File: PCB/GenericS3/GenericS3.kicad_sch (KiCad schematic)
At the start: 58 parts, among them J1 USB-C, J2 Shelly, P1 33, P10 42, P11 45, P12 46, P13 47, P14 48, P15 18, P16 19, P17 14, P18 15, P19 16, P2 34, P20 17, P21 6, P22 7, P23 8, P24 9, P25 20, P26 10, P27 11, P28 12, P29 13, P3 35, P30 1, P31 2, P32 3, P33 4, P34 5, P35 21, P36 43, P37 44, P38 0, P4 36, P5 37, P6 38, P7 39, P8 40, P9 41, U2 ESP32-S3-MINI-1, U5 MD8942

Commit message: Added GND pads
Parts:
- added P39, P40, P41, P42: ⏚, RevK:Square, symbol RevK:Square
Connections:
- net GND: now also P39.1 (P), P40.1 (P), P41.1 (P), P42.1 (P)
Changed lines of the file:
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@@
+    )
+  )
+  (symbol (lib_id "RevK:Square") (at 160.655 100.33 0) (unit 1)
+    (in_bom no) (on_board yes) (dnp no) (fields_autoplaced)
+    (property "Reference" "P42" (at 167.005 100.33 0)
+      (effects (font (size 1.27 1.27)) hide)
+    )
+    (property "Value" "⏚" (at 163.9062 100.33 0)
+      (effects (font (size 1.27 1.27)) (justify left))
+    )
+    (property "Footprint" "RevK:Square" (at 160.655 102.87 0)
+      (effects (font (size 1.27 1.27)) hide)
+    )
+    (property "Datasheet" "" (at 160.655 100.33 0)
+      (effects (font (size 1.27 1.27)) hide)
+    )
+    (pin "1")
+    (instances
+      (project "GenericS3"
+        (path "/2d210a96-f81f-42a9-8bf4-1b43c11086f3"
+          (reference "P42") (unit 1)
+        )
+      )
     )
   )
@@
         (path "/2d210a96-f81f-42a9-8bf4-1b43c11086f3"
           (reference "P11") (unit 1)
+        )
+      )
+    )
+  )
+  (symbol (lib_id "RevK:Square") (at 160.655 96.52 0) (unit 1)
+    (in_bom no) (on_board yes) (dnp no) (fields_autoplaced)
+    (property "Reference" "P41" (at 167.005 96.52 0)
+      (effects (font (size 1.27 1.27)) hide)
+    )
+    (property "Value" "⏚" (at 163.9062 96.52 0)
+      (effects (font (size 1.27 1.27)) (justify left))
+    )
+    (property "Footprint" "RevK:Square" (at 160.655 99.06 0)
+      (effects (font (size 1.27 1.27)) hide)
+    )
+    (property "Datasheet" "" (at 160.655 96.52 0)
+      (effects (font (size 1.27 1.27)) hide)
+    )
+    (pin "1")
+    (instances
+      (project "GenericS3"
+        (path "/2d210a96-f81f-42a9-8bf4-1b43c11086f3"
+          (reference "P41") (unit 1)
         )
       )
@@
     )
   )
+  (symbol (lib_id "power:GND") (at 160.655 88.9 270) (unit 1)
+    (in_bom yes) (on_board yes) (dnp no) (fields_autoplaced)
+    (property "Reference" "#PWR02" (at 154.305 88.9 0)
+      (effects (font (size 1.27 1.27)) hide)
+    )
+    (property "Value" "GND" (at 157.4801 88.9 90)
+      (effects (font (size 1.27 1.27)) (justify right))
+    )
+    (property "Footprint" "" (at 160.655 88.9 0)
+      (effects (font (size 1.27 1.27)) hide)
+    )
+    (property "Datasheet" "" (at 160.655 88.9 0)
+      (effects (font (size 1.27 1.27)) hide)
+    )
+    (pin "1")
+    (instances
+      (project "GenericS3"
+        (path "/2d210a96-f81f-42a9-8bf4-1b43c11086f3"
+          (reference "#PWR02") (unit 1)
+        )
+      )
+    )
+  )
   (symbol (lib_id "RevK:Round") (at 93.98 67.945 180) (unit 1)
     (in_bom no) (on_board yes) (dnp no)
@@
     )
   )
+  (symbol (lib_id "power:GND") (at 160.655 92.71 270) (unit 1)
+    (in_bom yes) (on_board yes) (dnp no) (fields_autoplaced)
+    (property "Reference" "#PWR05" (at 154.305 92.71 0)
+      (effects (font (size 1.27 1.27)) hide)
+    )
+    (property "Value" "GND" (at 157.4801 92.71 90)
+      (effects (font (size 1.27 1.27)) (justify right))
+    )
+    (property "Footprint" "" (at 160.655 92.71 0)
+      (effects (font (size 1.27 1.27)) hide)
+    )
+    (property "Datasheet" "" (at 160.655 92.71 0)
+      (effects (font (size 1.27 1.27)) hide)
+    )
+    (pin "1")
+    (instances
+      (project "GenericS3"
+        (path "/2d210a96-f81f-42a9-8bf4-1b43c11086f3"
+          (reference "#PWR05") (unit 1)
+        )
+      )
+    )
+  )
   (symbol (lib_id "RevK:VCUT") (at 250.19 169.545 0) (unit 1)
     (in_bom no) (on_board yes) (dnp no) (fields_autoplaced)
@@
     )
   )
+  (symbol (lib_id "power:GND") (at 160.655 96.52 270) (unit 1)
+    (in_bom yes) (on_board yes) (dnp no) (fields_autoplaced)
+    (property "Reference" "#PWR015" (at 154.305 96.52 0)
+      (effects (font (size 1.27 1.27)) hide)
+    )
+    (property "Value" "GND" (at 157.4801 96.52 90)
+      (effects (font (size 1.27 1.27)) (justify right))
+    )
+    (property "Footprint" "" (at 160.655 96.52 0)
+      (effects (font (size 1.27 1.27)) hide)
+    )
+    (property "Datasheet" "" (at 160.655 96.52 0)
+      (effects (font (size 1.27 1.27)) hide)
+    )
+    (pin "1")
+    (instances
+      (project "GenericS3"
+        (path "/2d210a96-f81f-42a9-8bf4-1b43c11086f3"
+          (reference "#PWR015") (unit 1)
+        )
+      )
+    )
+  )
   (symbol (lib_id "RevK:Round") (at 124.46 85.725 0) (unit 1)
     (in_bom no) (on_board yes) (dnp no) (fields_autoplaced)
@@
         (path "/2d210a96-f81f-42a9-8bf4-1b43c11086f3"
           (reference "P38") (unit 1)
+        )
+      )
+    )
+  )
+  (symbol (lib_id "RevK:Square") (at 160.655 92.71 0) (unit 1)
+    (in_bom no) (on_board yes) (dnp no) (fields_autoplaced)
+    (property "Reference" "P40" (at 167.005 92.71 0)
+      (effects (font (size 1.27 1.27)) hide)
+    )
+    (property "Value" "⏚" (at 163.9062 92.71 0)
+      (effects (font (size 1.27 1.27)) (justify left))
+    )
+    (property "Footprint" "RevK:Square" (at 160.655 95.25 0)
+      (effects (font (size 1.27 1.27)) hide)
+    )
+    (property "Datasheet" "" (at 160.655 92.71 0)
+      (effects (font (size 1.27 1.27)) hide)
+    )
+    (pin "1")
+    (instances
+      (project "GenericS3"
+        (path "/2d210a96-f81f-42a9-8bf4-1b43c11086f3"
+          (reference "P40") (unit 1)
         )
       )
@@
         (path "/825c70b0-4860-42b7-97dc-86bfa46e06fd"
           (reference "R7") (unit 1)
+        )
+      )
+    )
+  )
+  (symbol (lib_id "RevK:Square") (at 160.655 88.9 0) (unit 1)
+    (in_bom no) (on_board yes) (dnp no) (fields_autoplaced)
+    (property "Reference" "P39" (at 167.005 88.9 0)
+      (effects (font (size 1.27 1.27)) hide)
+    )
+    (property "Value" "⏚" (at 163.9062 88.9 0)
+      (effects (font (size 1.27 1.27)) (justify left))
+    )
+    (property "Footprint" "RevK:Square" (at 160.655 91.44 0)
+      (effects (font (size 1.27 1.27)) hide)
+    )
+    (property "Datasheet" "" (at 160.655 88.9 0)
+      (effects (font (size 1.27 1.27)) hide)
+    )
+    (pin "1")
+    (instances
+      (project "GenericS3"
+        (path "/2d210a96-f81f-42a9-8bf4-1b43c11086f3"
+          (reference "P39") (unit 1)
         )
       )
@@
         )
       )
+    )
+  )
+  (symbol (lib_id "power:GND") (at 160.655 100.33 270) (unit 1)
+    (in_bom yes) (on_board yes) (dnp no) (fields_autoplaced)
+    (property "Reference" "#PWR016" (at 154.305 100.33 0)
+      (effects (font (size 1.27 1.27)) hide)
+    )
+    (property "Value" "GND" (at 157.4801 100.33 90)
+      (effects (font (size 1.27 1.27)) (justify right))
+    )
+    (property "Footprint" "" (at 160.655 100.33 0)
+      (effects (font (size 1.27 1.27)) hide)
+    )
+    (property "Datasheet" "" (at 160.655 100.33 0)
+      (effects (font (size 1.27 1.27)) hide)
+    )
+    (pin "1")
+    (instances
+      (project "GenericS3"
+        (path "/2d210a96-f81f-42a9-8bf4-1b43c11086f3"
+          (reference "#PWR016") (unit 1)
+        )
+      )

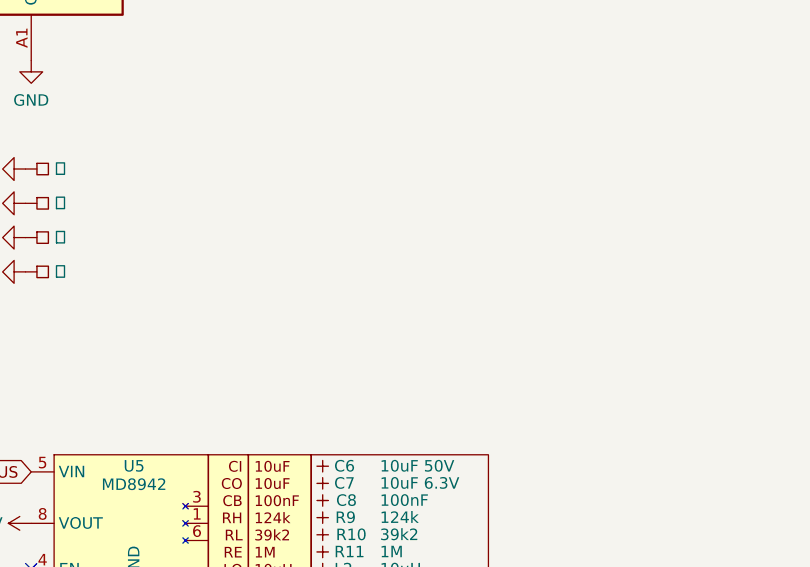
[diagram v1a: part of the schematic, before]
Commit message: Added connector
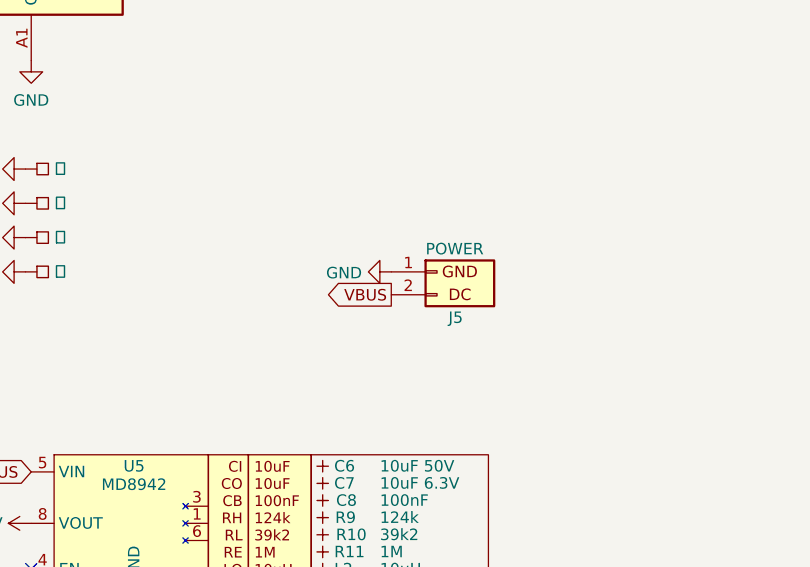
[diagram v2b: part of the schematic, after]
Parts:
- added J5: POWER, RevK:PTSM-HH1-2-RA, symbol RevK:PowerIn
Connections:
- net GND: now also J5.1 (GND)
- net VBUS: now also J5.2 (DC)
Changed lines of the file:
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@@
+    )
+  )
+  (global_label "VBUS" (shape output) (at 201.295 102.87 180) (fields_autoplaced)
+    (effects (font (size 1.27 1.27)) (justify right))
+    (property "Intersheetrefs" "${INTERSHEET_REFS}" (at 194.0654 102.87 0)
+      (effects (font (size 1.27 1.27)) (justify right) hide)
     )
   )
@@
     )
   )
+  (symbol (lib_id "RevK:PowerIn") (at 206.375 100.33 0) (unit 1)
+    (in_bom yes) (on_board yes) (dnp no)
+    (property "Reference" "J5" (at 207.645 105.41 0)
+      (effects (font (size 1.27 1.27)) (justify left))
+    )
+    (property "Value" "POWER" (at 205.105 97.79 0)
+      (effects (font (size 1.27 1.27)) (justify left))
+    )
+    (property "Footprint" "RevK:PTSM-HH1-2-RA" (at 206.375 100.33 0)
+      (effects (font (size 1.27 1.27)) hide)
+    )
+    (property "Datasheet" "~" (at 206.375 100.33 0)
+      (effects (font (size 1.27 1.27)) hide)
+    )
+    (pin "1")
+    (pin "2")
+    (instances
+      (project "Access"
+        (path "/2a267270-6585-45e3-a633-b53049f10066"
+          (reference "J5") (unit 1)
+        )
+      )
+      (project "GenericS3"
+        (path "/2d210a96-f81f-42a9-8bf4-1b43c11086f3"
+          (reference "J3") (unit 1)
+        )
+      )
+    )
+  )
   (symbol (lib_id "RevK:Round") (at 124.46 95.885 0) (unit 1)
     (in_bom no) (on_board yes) (dnp no) (fields_autoplaced)
@@
         )
       )
+    )
+  )
+  (symbol (lib_id "power:GND") (at 201.295 100.33 270) (unit 1)
+    (in_bom yes) (on_board yes) (dnp no)
+    (property "Reference" "#PWR045" (at 194.945 100.33 0)
+      (effects (font (size 1.27 1.27)) hide)
+    )
+    (property "Value" "GND" (at 198.0438 100.457 90)
+      (effects (font (size 1.27 1.27)) (justify right))
+    )
+    (property "Footprint" "" (at 201.295 100.33 0)
+      (effects (font (size 1.27 1.27)) hide)
+    )
+    (property "Datasheet" "" (at 201.295 100.33 0)
+      (effects (font (size 1.27 1.27)) hide)
+    )
+    (pin "1")
+    (instances
+      (project "Access"
+        (path "/2a267270-6585-45e3-a633-b53049f10066"
+          (reference "#PWR045") (unit 1)
+        )
+      )
+      (project "GenericS3"
+        (path "/2d210a96-f81f-42a9-8bf4-1b43c11086f3"
+          (reference "#PWR017") (unit 1)
+        )
+      )

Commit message: Diode
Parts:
- added D8: D, RevK:D_1206, symbol Device:D
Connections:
- net VBUS: no longer names the net of J1.A4 (VBUS), J1.A9 (VBUS), J1.B4 (VBUS), J1.B9 (VBUS)
- net VBUS: now also D8.2 (A); no longer J5.2 (DC), U5.5 (VIN)
- new net DC: D8.1 (K), J5.2 (DC), U5.5 (VIN)
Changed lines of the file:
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@@
     (stroke (width 0) (type default))
   )
-  (global_label "VBUS" (shape input) (at 161.29 122.555 180) (fields_autoplaced)
+  (global_label "DC" (shape input) (at 161.29 122.555 180) (fields_autoplaced)
     (effects (font (size 1.27 1.27)) (justify right))
-    (property "Intersheetrefs" "${INTERSHEET_REFS}" (at 154.1398 122.555 0)
+    (property "Intersheetrefs" "${INTERSHEET_REFS}" (at 156.419 122.555 0)
       (effects (font (size 1.27 1.27)) (justify right) hide)
     )
@@
     )
   )
-  (global_label "VBUS" (shape output) (at 176.53 38.735 0) (fields_autoplaced)
+  (global_label "DC" (shape output) (at 184.15 38.735 0) (fields_autoplaced)
     (effects (font (size 1.27 1.27)) (justify left))
-    (property "Intersheetrefs" "${INTERSHEET_REFS}" (at 183.6802 38.735 0)
+    (property "Intersheetrefs" "${INTERSHEET_REFS}" (at 189.021 38.735 0)
       (effects (font (size 1.27 1.27)) (justify left) hide)
     )
@@
     )
   )
-  (global_label "VBUS" (shape output) (at 201.295 102.87 180) (fields_autoplaced)
+  (global_label "DC" (shape output) (at 201.295 102.87 180) (fields_autoplaced)
     (effects (font (size 1.27 1.27)) (justify right))
-    (property "Intersheetrefs" "${INTERSHEET_REFS}" (at 194.0654 102.87 0)
+    (property "Intersheetrefs" "${INTERSHEET_REFS}" (at 196.424 102.87 0)
       (effects (font (size 1.27 1.27)) (justify right) hide)
     )
@@
         )
       )
+    )
+  )
+  (symbol (lib_id "Device:D") (at 180.34 38.735 180) (unit 1)
+    (in_bom yes) (on_board yes) (dnp no)
+    (property "Reference" "D8" (at 180.34 33.2232 0)
+      (effects (font (size 1.27 1.27)))
+    )
+    (property "Value" "D" (at 180.34 35.5346 0)
+      (effects (font (size 1.27 1.27)))
+    )
+    (property "Footprint" "RevK:D_1206" (at 180.34 38.735 0)
+      (effects (font (size 1.27 1.27)) hide)
+    )
+    (property "Datasheet" "~" (at 180.34 38.735 0)
+      (effects (font (size 1.27 1.27)) hide)
+    )
+    (property "LCSC Part #" "C143805" (at 180.34 38.735 0)
+      (effects (font (size 1.27 1.27)) hide)
+    )
+    (pin "1")
+    (pin "2")
+    (instances
+      (project "Access"
+        (path "/2a267270-6585-45e3-a633-b53049f10066"
+          (reference "D8") (unit 1)
+        )
+      )
+      (project "GenericS3"
+        (path "/2d210a96-f81f-42a9-8bf4-1b43c11086f3"
+          (reference "D1") (unit 1)
+        )
+      )

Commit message: Remove socket from BOM
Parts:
- J5: now left out of the parts list
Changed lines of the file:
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@@
   )
   (symbol (lib_id "RevK:PowerIn") (at 206.375 100.33 0) (unit 1)
-    (in_bom yes) (on_board yes) (dnp no)
+    (in_bom no) (on_board yes) (dnp no)
     (property "Reference" "J5" (at 207.645 105.41 0)
       (effects (font (size 1.27 1.27)) (justify left))
